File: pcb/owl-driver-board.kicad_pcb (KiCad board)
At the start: 2 copper layers, 65 x 56 mm, 178 parts, among them J1 CONN_04, J10 1890963, J11 ENABLE, J2 RASPBERRYPI-40-PIN-GPIO, J3 1890963, J4 1890963, J5 1890963, J6 CONN_04X2, J7 1890963, J8 1890963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

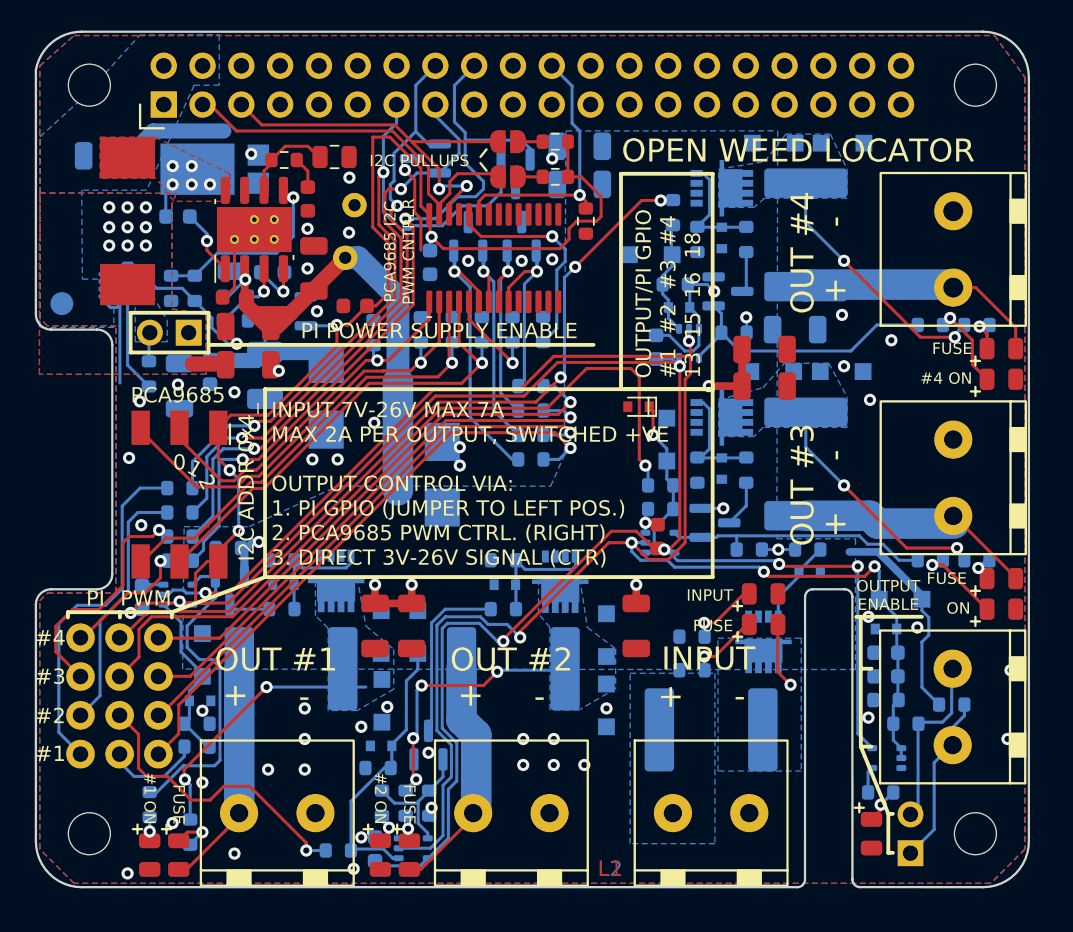
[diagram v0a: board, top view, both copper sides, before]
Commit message: 4-way board, revision v2.5
Bump the revision with some small tweaks -
 - Lower profile Phoenix Contact screw terminals - replace 1890963 with 1935161 (C3819953)
 - 10k discharge resistor across all outputs to reduce ghost voltages
 - Format updates for KiCad 9
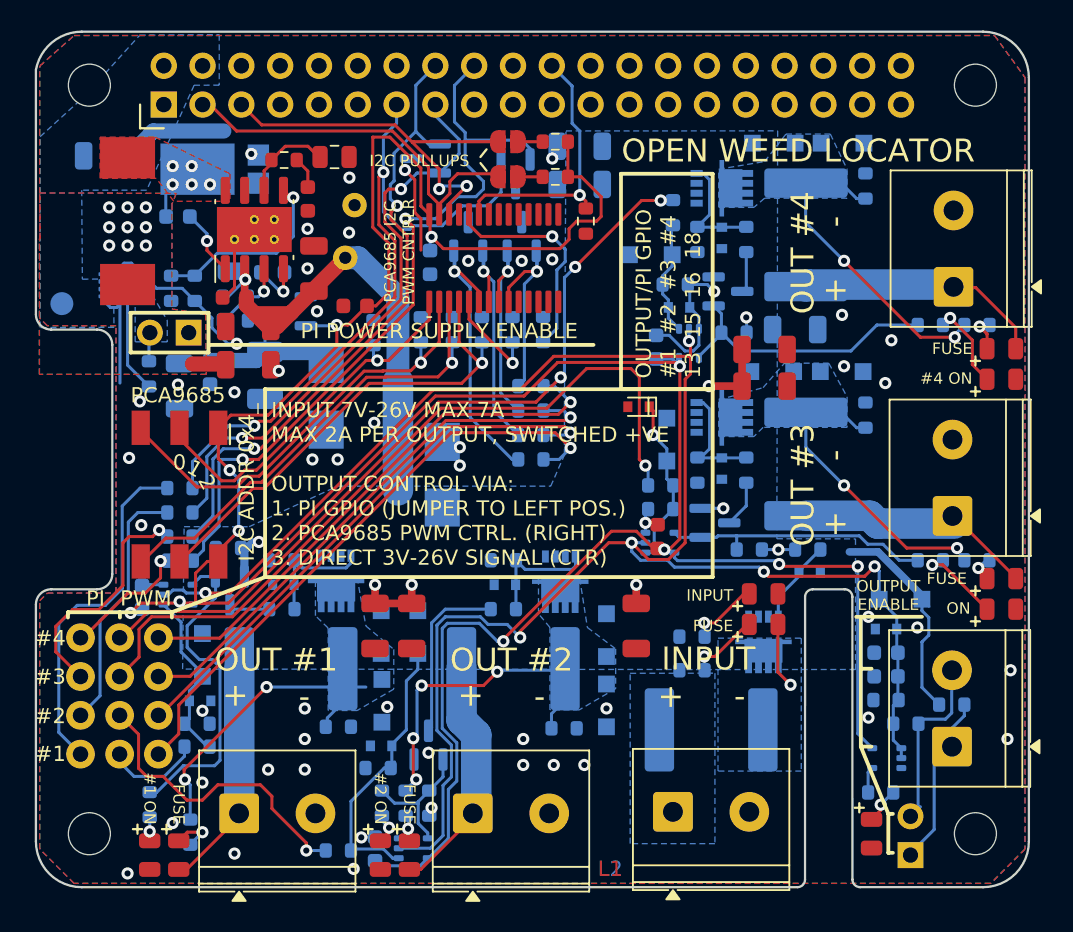
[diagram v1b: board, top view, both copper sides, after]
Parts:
- added R59: 10k, Resistor_SMD:R_0603_1608Metric, B.Cu at (54.3, 10.6)
- added R60: 10k, Resistor_SMD:R_0603_1608Metric, B.Cu at (54.3, 25.6)
- added R61: 10k, Resistor_SMD:R_0603_1608Metric, B.Cu at (34.6, 46.1)
- added R62: 10k, Resistor_SMD:R_0603_1608Metric, B.Cu at (19.8, 46.0)
- D17, D18, D2, D3, D6: value BZT52C5V1T -> BZT585B13T-7 13V
- J10, J3, J4, J5, J7, J8: value 1890963 -> 1935161; footprint misc:Connector_Phoenix-Contact_MKDSN_1890963_P5.0_2x -> TerminalBlock_Phoenix:TerminalBlock_Phoenix_PT-1,5-2-5.0-H_1x02_P5.00mm_Horizontal
- moved J10 5.45 mm to (60.0, 47.3)
- moved J3 5.44 mm to (41.7, 51.6)
- moved J7 5.41 mm to (60.0, 32.2)
- moved J5 5.36 mm to (28.6, 51.7)
- moved J4 5.35 mm to (13.3, 51.7)
- moved J8 5.33 mm to (60.1, 17.2)
- moved LOGO1 0.70 mm to (57.2, 29.8)
- moved J11 0.12 mm to (57.2, 54.4)
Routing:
- net /M1_D: track 17.6 -> 19.4 mm
- net /M4_D: track 16.5 -> 18.1 mm
- net /M3_D: track 14.9 -> 16.5 mm
- net /M2_D: track 17.2 -> 18.8 mm
- net MOSFET2: track 19.5 -> 20.1 mm
- net GND: vias 59 -> 57
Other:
- board text added: "2025-01-13"
- board text added: "HAL lead-free"
- board text added: "v2.5"
- board text removed: "2024-06-08"
- board text removed: "ENIG"
- board text removed: "v2.4"
